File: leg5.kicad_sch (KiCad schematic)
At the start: 12 parts, among them J14 Leg5 Motor1, J15 Leg5 Motor2, J16 Leg5 Motor3

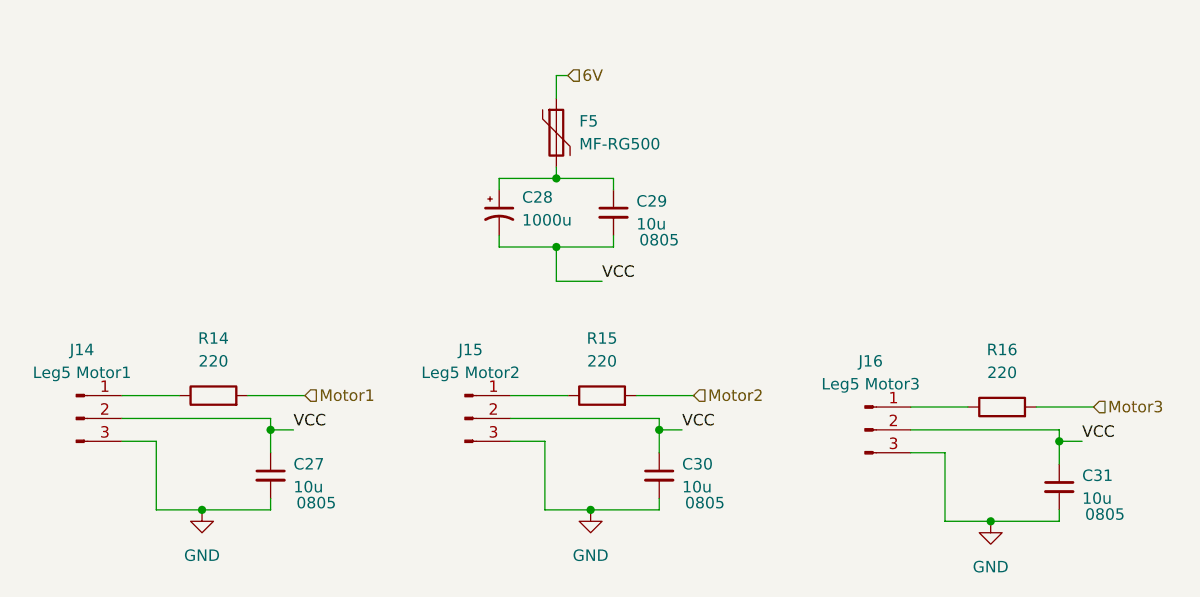
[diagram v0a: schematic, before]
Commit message: removed crystal, fixed caps
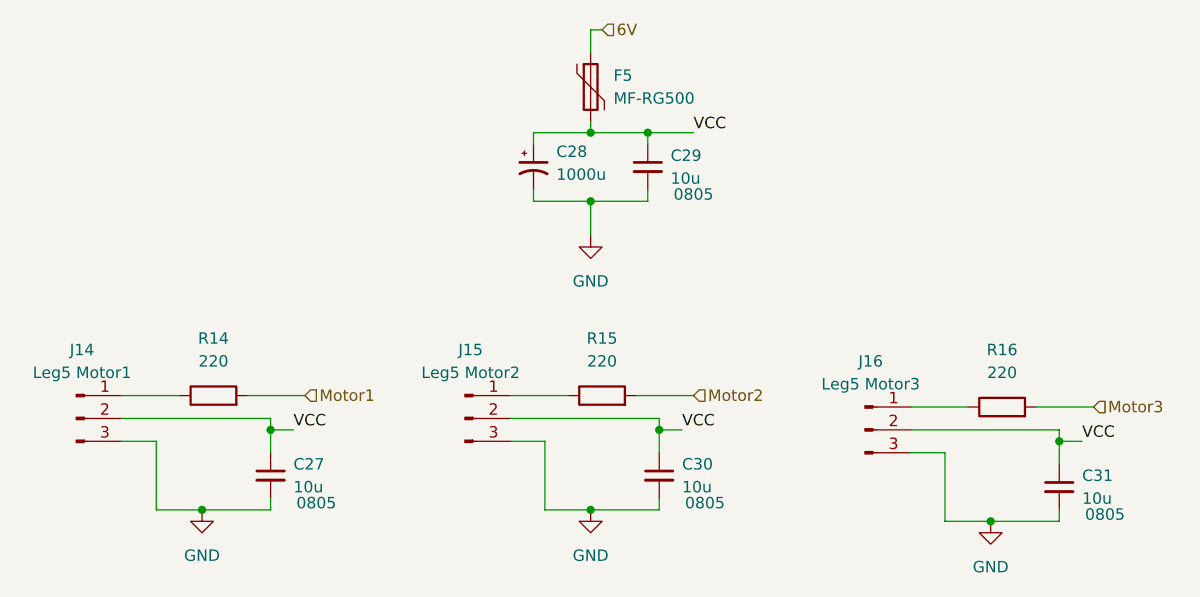
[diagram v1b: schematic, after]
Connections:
- net GND: now also C28.2, C29.2
- net VCC: now also C28.1, C29.1, F5.2; no longer C28.2, C29.2
